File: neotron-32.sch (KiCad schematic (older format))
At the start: 12 parts, among them J1 Conn_02x06, J2 Conn_02x06, J3 Conn_02x04, U1 TM4C123G_Launchpad

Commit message: Swapped Wifi pin header for socket.
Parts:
- added H5, H6: MountingHole, MountingHole:MountingHole_3.2mm_M3, symbol Mechanical:MountingHole
- J3: footprint Connector_PinHeader_2.54mm:PinHeader_2x04_P2.54mm_Vertical -> Connector_PinSocket_2.54mm:PinSocket_2x04_P2.54mm_Vertical
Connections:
- net +3V3: now also J3.1 (Pin_1); no longer J3.2 (Pin_2)
- net GND: now also J3.8 (Pin_8); no longer J3.7 (Pin_7)
- net PD6_U2RX: now also J3.7 (Pin_7); no longer J3.8 (Pin_8)
- net PD7_U2TX: now also J3.2 (Pin_2); no longer J3.1 (Pin_1)
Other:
- moved on the sheet: H1, H2, H3, H4
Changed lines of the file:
@@
 Sheet 1 10
 Title "Neotron 32K Main PCB"
-Date "2019-12-16"
+Date "2020-01-18"
 Rev "[Uncontrolled]"
 Comp "github.com/neotron-compute/Neotron-32-Hardware"
@@
 L Connector_Generic:Conn_02x04_Odd_Even J3
 U 1 1 5E4EF859
-P 8950 2950
-F 0 "J3" H 9000 3267 50  0000 C CNN
-F 1 "Conn_02x04" H 9000 3176 50  0000 C CNN
-F 2 "Connector_PinHeader_2.54mm:PinHeader_2x04_P2.54mm_Vertical" H 8950 2950 50  0001 C CNN
-F 3 "~" H 8950 2950 50  0001 C CNN
-F 4 "~" H 0   0   50  0001 C CNN "Manufacturer"
-F 5 "~" H 0   0   50  0001 C CNN "PartNo"
-	1    8950 2950
-	1    0    0    -1
+P 9050 2950
+F 0 "J3" H 9100 3267 50  0000 C CNN
+F 1 "Conn_02x04" H 9100 3176 50  0000 C CNN
+F 2 "Connector_PinSocket_2.54mm:PinSocket_2x04_P2.54mm_Vertical" H 9050 2950 50  0001 C CNN
+F 3 "~" H 9050 2950 50  0001 C CNN
+F 4 "~" H 100 0   50  0001 C CNN "Manufacturer"
+F 5 "~" H 100 0   50  0001 C CNN "PartNo"
+	1    9050 2950
+	-1   0    0    -1
 $EndComp
 Text Label 8700 2850 2    50   ~ 0
@@
 L Mechanical:MountingHole H1
 U 1 1 5DFC719B
+P 6200 6600
+F 0 "H1" H 6300 6646 50  0000 L CNN
+F 1 "MountingHole" H 6300 6555 50  0000 L CNN
+F 2 "MountingHole:MountingHole_3.2mm_M3" H 6200 6600 50  0001 C CNN
+F 3 "~" H 6200 6600 50  0001 C CNN
+F 4 "~" H 4650 -300 50  0001 C CNN "Manufacturer"
+F 5 "~" H 4650 -300 50  0001 C CNN "PartNo"
+	1    6200 6600
+	1    0    0    -1
+$EndComp
+$Comp
+L Mechanical:MountingHole H2
+U 1 1 5DFC7744
 P 6200 6800
-F 0 "H1" H 6300 6846 50  0000 L CNN
+F 0 "H2" H 6300 6846 50  0000 L CNN
 F 1 "MountingHole" H 6300 6755 50  0000 L CNN
 F 2 "MountingHole:MountingHole_3.2mm_M3" H 6200 6800 50  0001 C CNN
 F 3 "~" H 6200 6800 50  0001 C CNN
-F 4 "~" H 4650 -100 50  0001 C CNN "Manufacturer"
-F 5 "~" H 4650 -100 50  0001 C CNN "PartNo"
+F 4 "~" H 4650 -300 50  0001 C CNN "Manufacturer"
+F 5 "~" H 4650 -300 50  0001 C CNN "PartNo"
 	1    6200 6800
 	1    0    0    -1
 $EndComp
 $Comp
-L Mechanical:MountingHole H2
-U 1 1 5DFC7744
+L Mechanical:MountingHole H3
+U 1 1 5DFC781B
 P 6200 7000
-F 0 "H2" H 6300 7046 50  0000 L CNN
+F 0 "H3" H 6300 7046 50  0000 L CNN
 F 1 "MountingHole" H 6300 6955 50  0000 L CNN
 F 2 "MountingHole:MountingHole_3.2mm_M3" H 6200 7000 50  0001 C CNN
 F 3 "~" H 6200 7000 50  0001 C CNN
-F 4 "~" H 4650 -100 50  0001 C CNN "Manufacturer"
-F 5 "~" H 4650 -100 50  0001 C CNN "PartNo"
+F 4 "~" H 4650 -300 50  0001 C CNN "Manufacturer"
+F 5 "~" H 4650 -300 50  0001 C CNN "PartNo"
 	1    6200 7000
 	1    0    0    -1
 $EndComp
 $Comp
-L Mechanical:MountingHole H3
-U 1 1 5DFC781B
+L Mechanical:MountingHole H4
+U 1 1 5DFC799C
 P 6200 7200
-F 0 "H3" H 6300 7246 50  0000 L CNN
+F 0 "H4" H 6300 7246 50  0000 L CNN
 F 1 "MountingHole" H 6300 7155 50  0000 L CNN
 F 2 "MountingHole:MountingHole_3.2mm_M3" H 6200 7200 50  0001 C CNN
 F 3 "~" H 6200 7200 50  0001 C CNN
-F 4 "~" H 4650 -100 50  0001 C CNN "Manufacturer"
-F 5 "~" H 4650 -100 50  0001 C CNN "PartNo"
+F 4 "~" H 4650 -300 50  0001 C CNN "Manufacturer"
+F 5 "~" H 4650 -300 50  0001 C CNN "PartNo"
 	1    6200 7200
 	1    0    0    -1
 $EndComp
-$Comp
-L Mechanical:MountingHole H4
-U 1 1 5DFC799C
+Text Label 1500 2550 0    50   ~ 0
+PA2_SPI_CLK
+Text Label 3000 2150 0    50   ~ 0
+PC4_U1RTS
+Wire Wire Line
+	1400 2650 2100 2650
+Entry Wire Line
+	2100 2650 2200 2750
+Wire Wire Line
+	8150 1150 8150 2050
+Wire Wire Line
+	8150 2150 8150 2350
+Entry Wire Line
+	9950 1550 10050 1650
+Entry Wire Line
+	9950 2550 10050 2650
+Text Label 8750 2250 2    50   ~ 0
+~RESET
+Text Label 8750 1250 2    50   ~ 0
+~RESET
+Wire Wire Line
+	8250 2250 8250 2550
+Wire Wire Line
+	8250 2250 8750 2250
+Wire Wire Line
+	8250 2550 9950 2550
+Wire Wire Line
+	8250 1250 8250 1550
+Wire Wire Line
+	8250 1250 8750 1250
+Wire Wire Line
+	8250 1550 9950 1550
+Text Notes 550  7700 0    50   Italic 0
+The Neotron-32 is based around a Texas Instruments EK-TM4C123GH6 Tiva-C Launchpad board. This includes a TM4C123 microcontroller\nand a JTAG + USB Serial interface.\n\nDrill down into the sub-sheets to see more detail.
+$Comp
+L Mechanical:MountingHole H5
+U 1 1 5E157BE6
 P 6200 7400
-F 0 "H4" H 6300 7446 50  0000 L CNN
+F 0 "H5" H 6300 7446 50  0000 L CNN
 F 1 "MountingHole" H 6300 7355 50  0000 L CNN
 F 2 "MountingHole:MountingHole_3.2mm_M3" H 6200 7400 50  0001 C CNN
@@
 	1    0    0    -1
 $EndComp
-Text Label 1500 2550 0    50   ~ 0
-PA2_SPI_CLK
-Text Label 3000 2150 0    50   ~ 0
-PC4_U1RTS
-Wire Wire Line
-	1400 2650 2100 2650
-Entry Wire Line
-	2100 2650 2200 2750
-Wire Wire Line
-	8150 1150 8150 2050
-Wire Wire Line
-	8150 2150 8150 2350
-Entry Wire Line
-	9950 1550 10050 1650
-Entry Wire Line
-	9950 2550 10050 2650
-Text Label 8750 2250 2    50   ~ 0
-~RESET
-Text Label 8750 1250 2    50   ~ 0
-~RESET
-Wire Wire Line
-	8250 2250 8250 2550
-Wire Wire Line
-	8250 2250 8750 2250
-Wire Wire Line
-	8250 2550 9950 2550
-Wire Wire Line
-	8250 1250 8250 1550
-Wire Wire Line
-	8250 1250 8750 1250
-Wire Wire Line
-	8250 1550 9950 1550
-Text Notes 550  7700 0    50   Italic 0
-The Neotron-32 is based around a Texas Instruments EK-TM4C123GH6 Tiva-C Launchpad board. This includes a TM4C123 microcontroller\nand a JTAG + USB Serial interface.\n\nDrill down into the sub-sheets to see more detail.
+$Comp
+L Mechanical:MountingHole H6
+U 1 1 5E1640CD
+P 6200 7600
+F 0 "H6" H 6300 7646 50  0000 L CNN
+F 1 "MountingHole" H 6300 7555 50  0000 L CNN
+F 2 "MountingHole:MountingHole_3.2mm_M3" H 6200 7600 50  0001 C CNN
+F 3 "~" H 6200 7600 50  0001 C CNN
+F 4 "~" H 4650 100 50  0001 C CNN "Manufacturer"
+F 5 "~" H 4650 100 50  0001 C CNN "PartNo"
+	1    6200 7600
+	1    0    0    -1
+$EndComp
 Wire Bus Line
 	8150 2900 8150 3450

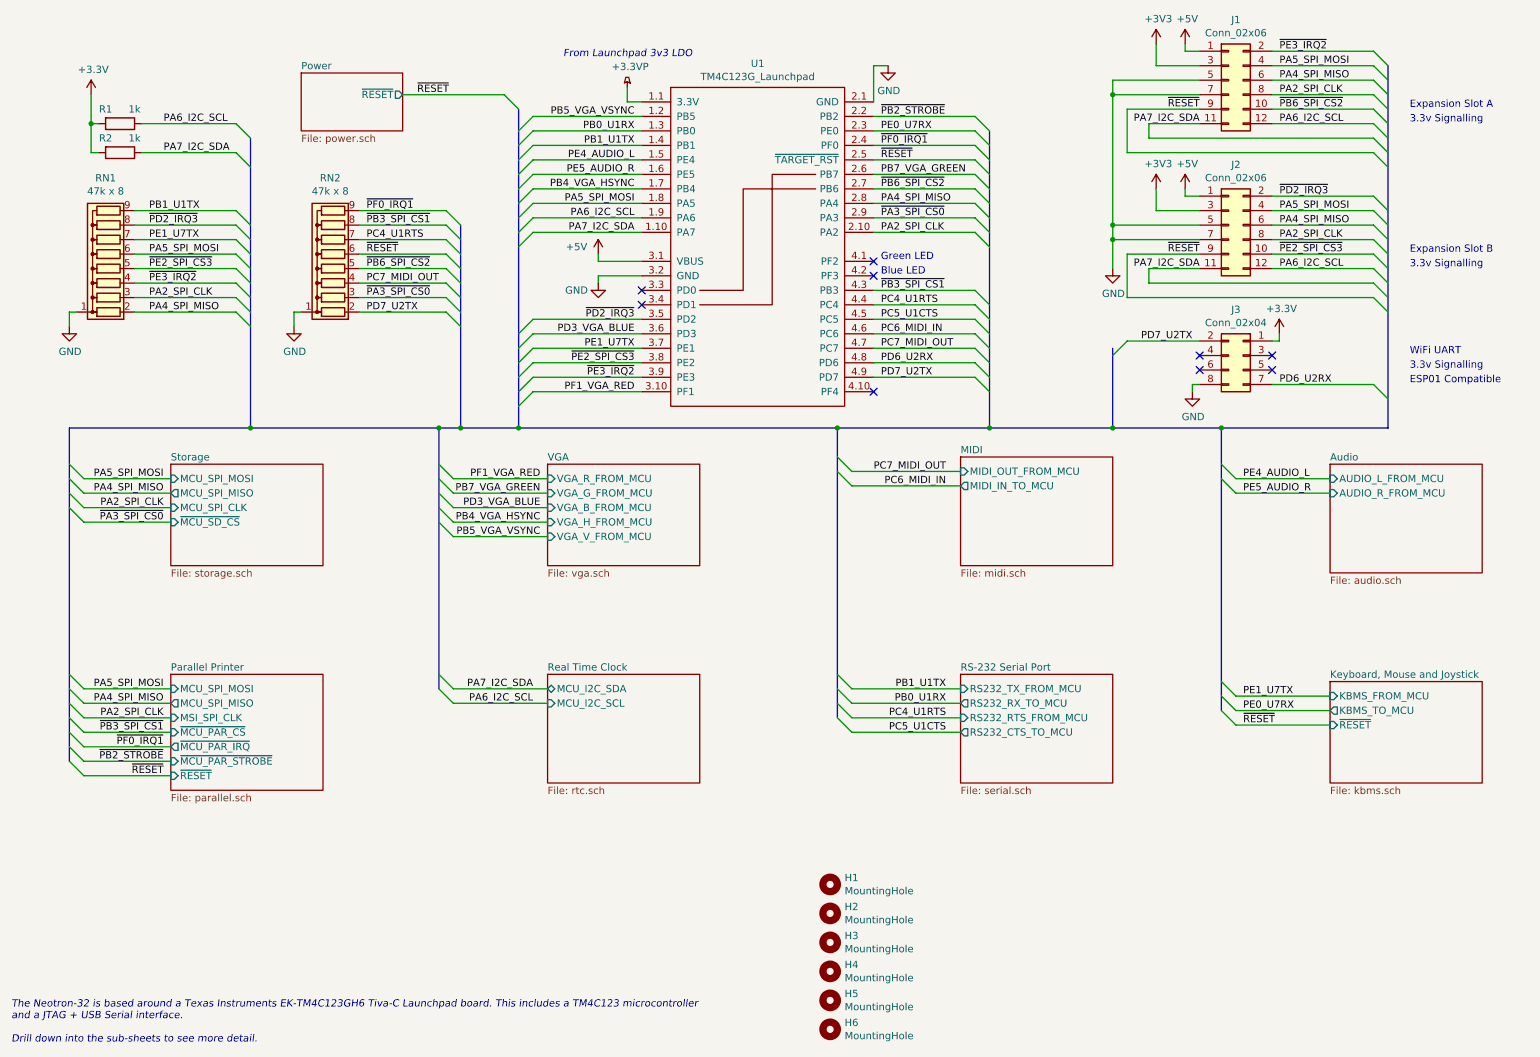
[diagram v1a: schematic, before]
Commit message: Bug fixes part 1.
* Added XTAL to Atmega.
* Added UART header to Atmega.
* Added page numbers.
* Removed the 470R in favour of 330R (to rationalise the BOM)
* Replaced MAX3232 caps with 100n
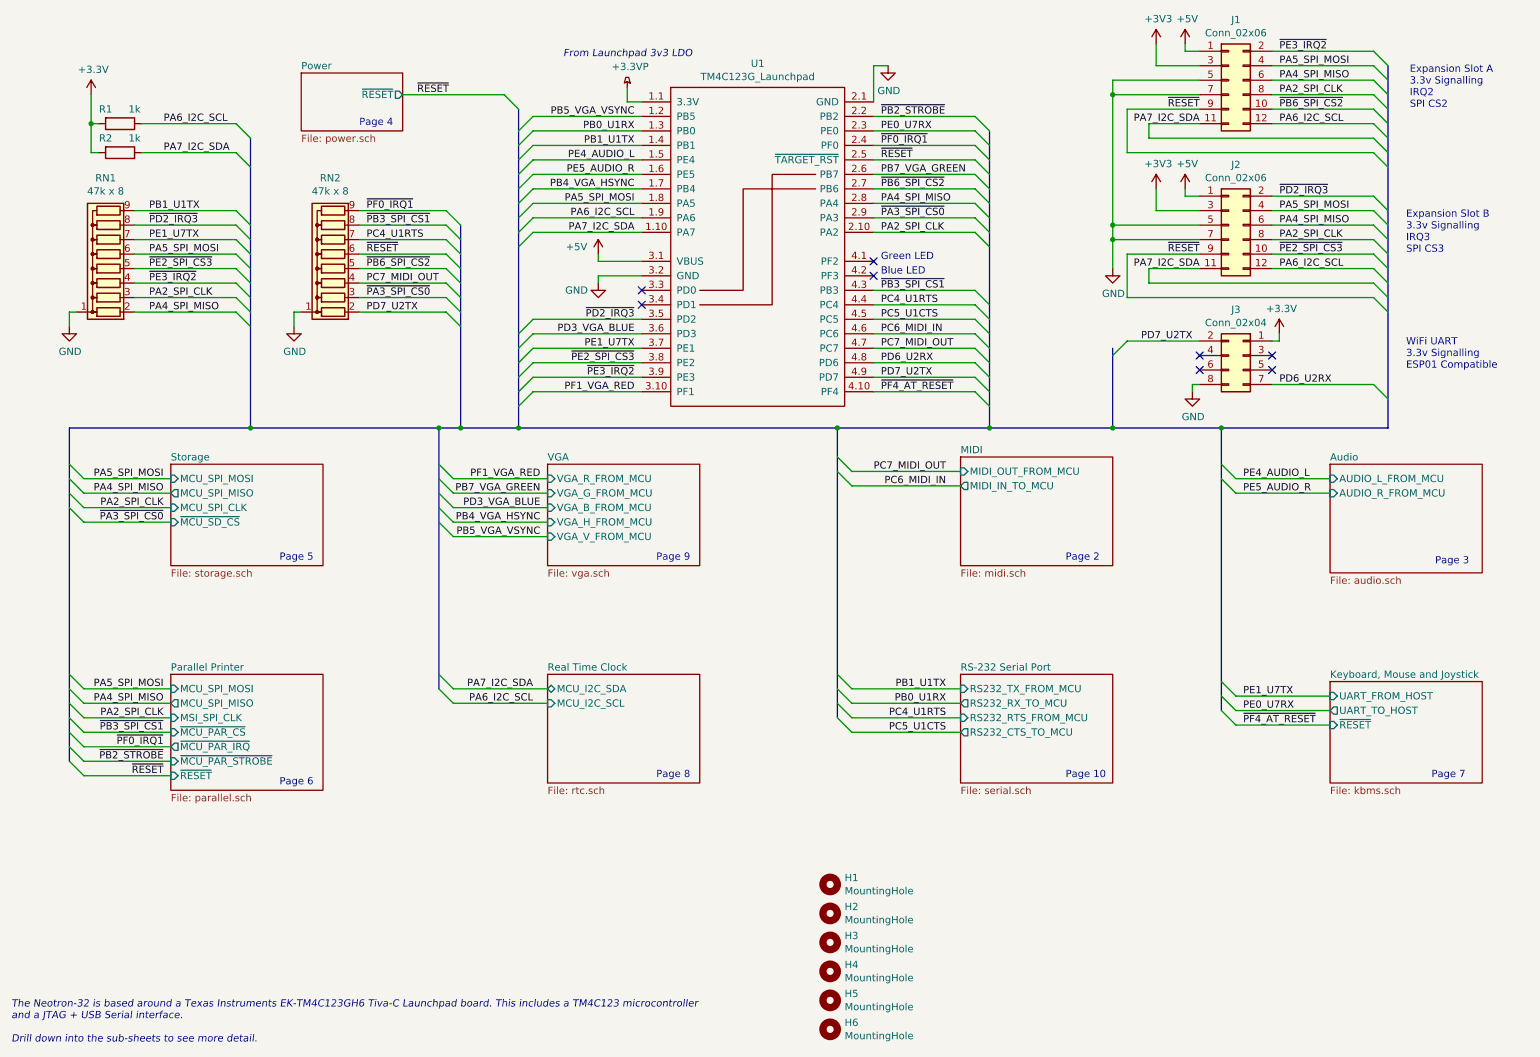
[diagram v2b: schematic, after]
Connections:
- net ~PF4_AT_RESET: now reaches U1.4.10 (PF4)
- no-connect marks 9 -> 8
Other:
- note added: "Expansion Slot A\n3.3v Signalling\nIRQ2\nSPI CS2"
- note added: "Expansion Slot B\n3.3v Signalling\nIRQ3\nSPI CS3"
- note added: "Page 10"
- note added: "Page 2"
- note added: "Page 3"
- note added: "Page 4"
- note added: "Page 5"
- note added: "Page 6"
- note added: "Page 7"
- note added: "Page 8"
- note added: "Page 9"
- note added: "WiFi UART\n3.3v Signalling\nESP01 Compatible"
- note removed: "3.3v Signalling"
- note removed: "ESP01 Compatible"
- note removed: "Expansion Slot A"
- note removed: "Expansion Slot B"
- note removed: "WiFi UART"
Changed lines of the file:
@@
 Sheet 1 10
 Title "Neotron 32K Main PCB"
-Date "2020-01-18"
+Date "2020-03-29"
 Rev "[Uncontrolled]"
 Comp "github.com/neotron-compute/Neotron-32-Hardware"
@@
 F0 "Keyboard, Mouse and Joystick" 50
 F1 "kbms.sch" 50
-F2 "KBMS_FROM_MCU" I L 9650 5300 50
-F3 "KBMS_TO_MCU" O L 9650 5400 50
+F2 "UART_FROM_HOST" I L 9650 5300 50
+F3 "UART_TO_HOST" O L 9650 5400 50
 F4 "~RESET" I L 9650 5500 50
 $EndSheet
@@
 PE1_U7TX
 Text Label 9050 5500 0    50   ~ 0
-~RESET
+~PF4_AT_RESET
 Text Label 7000 5350 2    50   ~ 0
 PB0_U1RX
@@
 Text Label 9300 1850 0    50   ~ 0
 ~PD2_IRQ3
-NoConn ~ 6500 3200
 Wire Wire Line
 	2100 1550 1450 1550
@@
 	9950 3150 10050 3250
 Text Notes 10200 1250 0    50   ~ 0
-Expansion Slot A
-Text Notes 10200 2250 0    50   ~ 0
-Expansion Slot B
-Text Notes 10200 2950 0    50   ~ 0
-WiFi UART
+Expansion Slot A\n3.3v Signalling\nIRQ2\nSPI CS2
+Text Notes 10175 3050 0    50   ~ 0
+WiFi UART\n3.3v Signalling\nESP01 Compatible
 $Comp
 L Connector_Generic:Conn_02x04_Odd_Even J3
@@
 Text Label 3000 2650 0    50   ~ 0
 PD7_U2TX
-Text Notes 10200 1350 0    50   ~ 0
-3.3v Signalling
-Text Notes 10200 2350 0    50   ~ 0
-3.3v Signalling
-Text Notes 10200 3050 0    50   ~ 0
-3.3v Signalling
-Text Notes 10200 3150 0    50   ~ 0
-ESP01 Compatible
 $Comp
 L Mechanical:MountingHole H1
@@
 	1    0    0    -1
 $EndComp
+Text Notes 2950 1375 0    50   ~ 0
+Page 4
+Text Notes 2400 4375 0    50   ~ 0
+Page 5
+Text Notes 2400 5925 0    50   ~ 0
+Page 6
+Text Notes 5000 5875 0    50   ~ 0
+Page 8
+Text Notes 5000 4375 0    50   ~ 0
+Page 9
+Text Notes 7825 4375 0    50   ~ 0
+Page 2
+Text Notes 7825 5875 0    50   ~ 0
+Page 10
+Text Notes 10375 4400 0    50   ~ 0
+Page 3
+Text Notes 10350 5875 0    50   ~ 0
+Page 7
+Text Notes 10175 2250 0    50   ~ 0
+Expansion Slot B\n3.3v Signalling\nIRQ3\nSPI CS3
+Entry Wire Line
+	7200 3200 7300 3300
+Wire Wire Line
+	6500 3200 7200 3200
 Wire Bus Line
 	8150 2900 8150 3450
@@
 Wire Bus Line
 	10050 950  10050 3450
+Text Label 6550 3200 0    50   ~ 0
+~PF4_AT_RESET
 $EndSCHEMATC
